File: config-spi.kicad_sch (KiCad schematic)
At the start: 40 parts, among them J1 878321412, Q7 BSS138APW, Q8 BSS138APW, U15 XC7K160T-FFG676, U3 S25FL128SAGNFI000

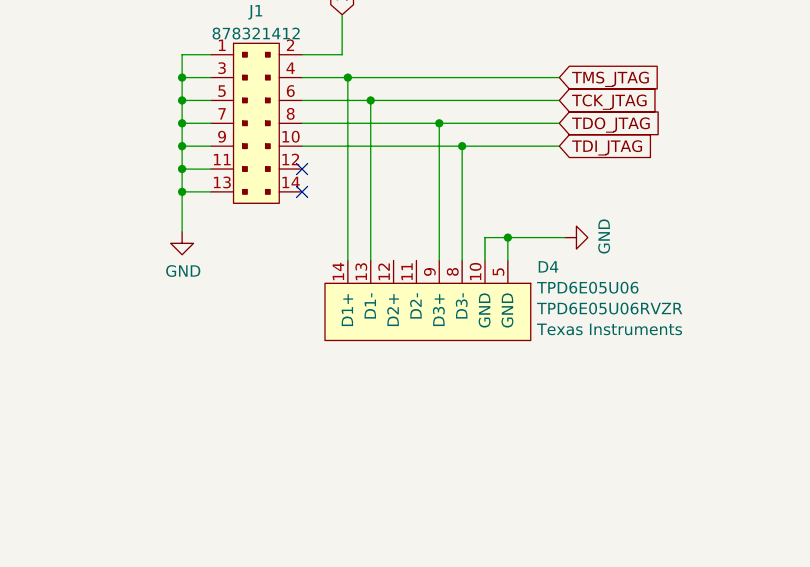
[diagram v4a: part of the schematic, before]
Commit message: Implement LED and PB mechanical concept. Assign bank 15 to FMC, remove buttons and add new ones
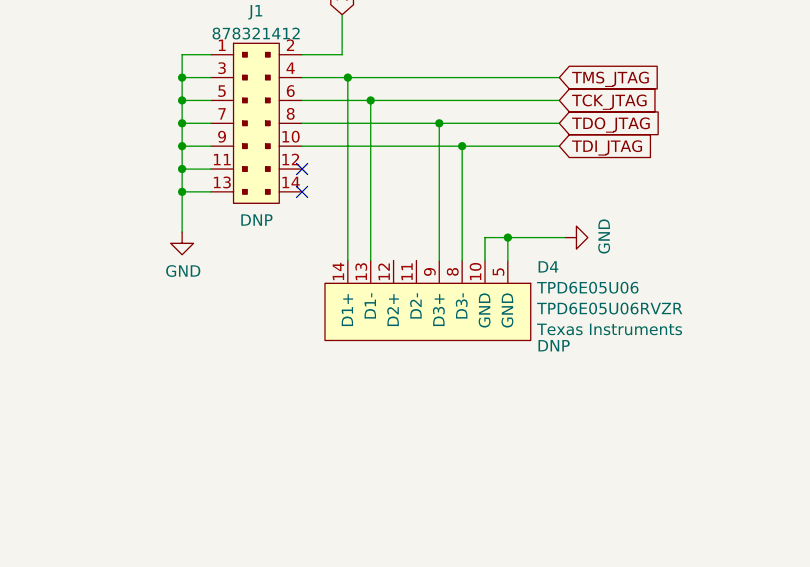
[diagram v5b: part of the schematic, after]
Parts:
- D4, J1: DNP (none) -> DNP
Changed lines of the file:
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@@
       (effects (font (size 1.27 1.27)) (justify right))
     )
+    (property "DNP" "DNP" (id 6) (at 78.105 259.715 90))
     (pin "10")
     (pin "11")
@@
   )
   (symbol (lib_id "antmicroRectangularConnectorsHeadersMalePins:878321412") (at 45.085 234.95 0) (unit 1)
-    (in_bom yes) (on_board yes) (fields_autoplaced)
+    (in_bom yes) (on_board yes)
     (property "Reference" "J1" (id 0) (at 45.085 222.4872 0))
     (property "Value" "878321412" (id 1) (at 45.085 225.0241 0))
@@
       (effects (font (size 1.524 1.524)) (justify left) hide)
     )
+    (property "DNP" "DNP" (id 6) (at 45.085 245.745 0))
     (pin "1")
     (pin "10")

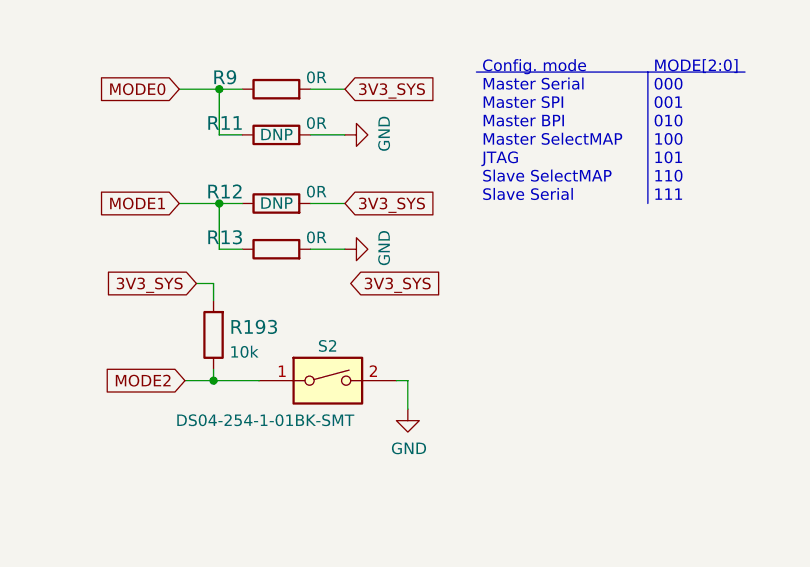
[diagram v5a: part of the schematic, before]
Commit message: Improve mechanical concept
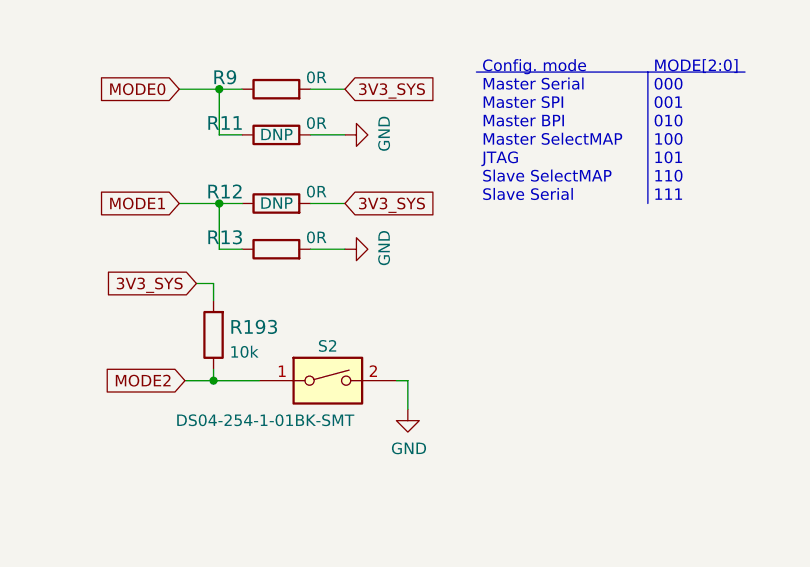
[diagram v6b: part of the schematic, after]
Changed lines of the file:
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@@
-    )
-  )
-  (global_label "3V3_SYS" (shape input) (at 241.3 252.095 0) (fields_autoplaced)
-    (effects (font (size 1.27 1.27)) (justify left))
-    (property "Intersheet References" "${INTERSHEET_REFS}" (id 0) (at 0 0 0)
-      (effects (font (size 1.27 1.27)) hide)
     )
   )

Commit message: Length match and deskew Die 7, Die3, command, control and addres. Modify SPI Flash footprint
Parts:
- U3: footprint data-center-dram-tester-footprints:S25FL128SAGNFI000 -> antmicro-footprints:WSON8x6_WSON6x5_dual
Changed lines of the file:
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@@
       (effects (font (size 1.524 1.524)))
     )
-    (property "Footprint" "data-center-dram-tester-footprints:S25FL128SAGNFI000" (id 2) (at 80.645 96.774 0)
+    (property "Footprint" "antmicro-footprints:WSON8x6_WSON6x5_dual" (id 2) (at 80.645 96.774 0)
       (effects (font (size 1.524 1.524)) hide)
     )
